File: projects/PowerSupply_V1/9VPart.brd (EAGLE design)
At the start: 49.5 x 58.4 mm, 24 parts, among them IC1 LM2596T, IC2 LM2596T, X1 IN, X2 OUT

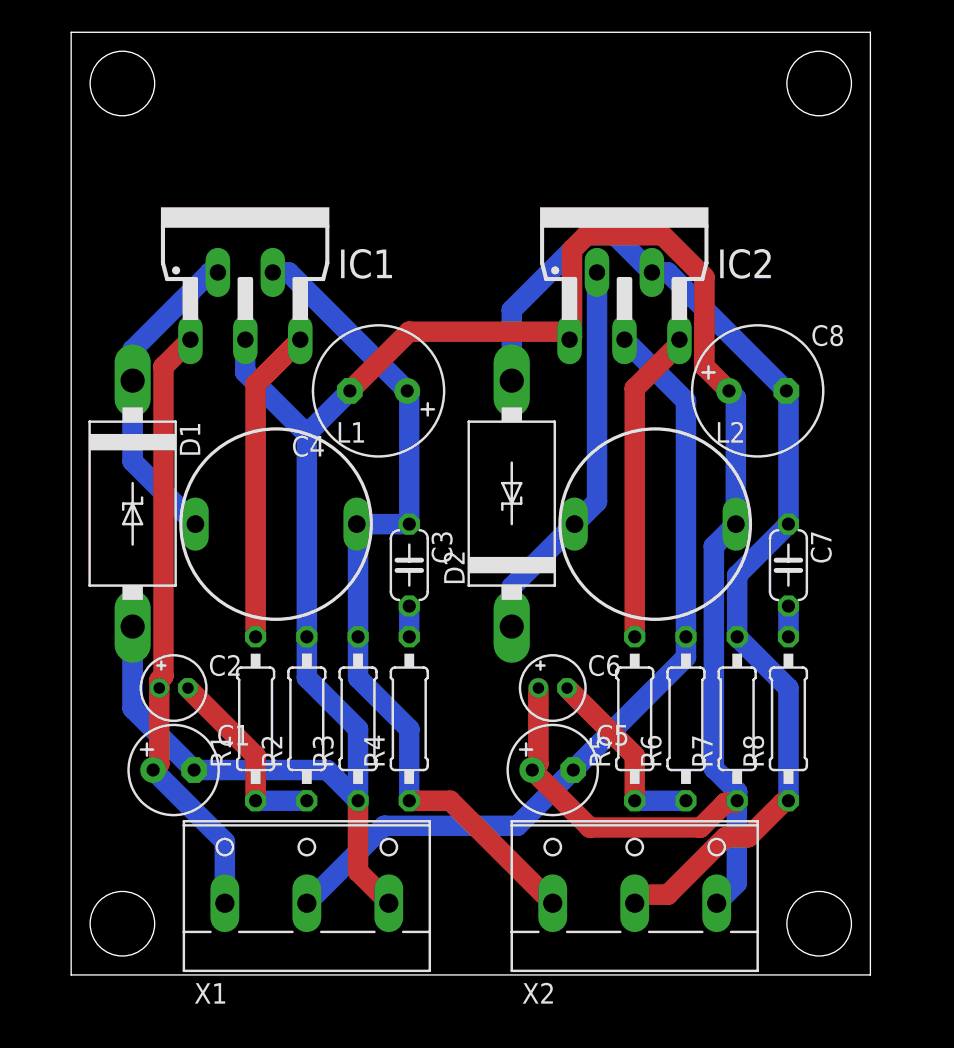
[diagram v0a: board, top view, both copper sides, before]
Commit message: refactor(all): schematics and routing changed
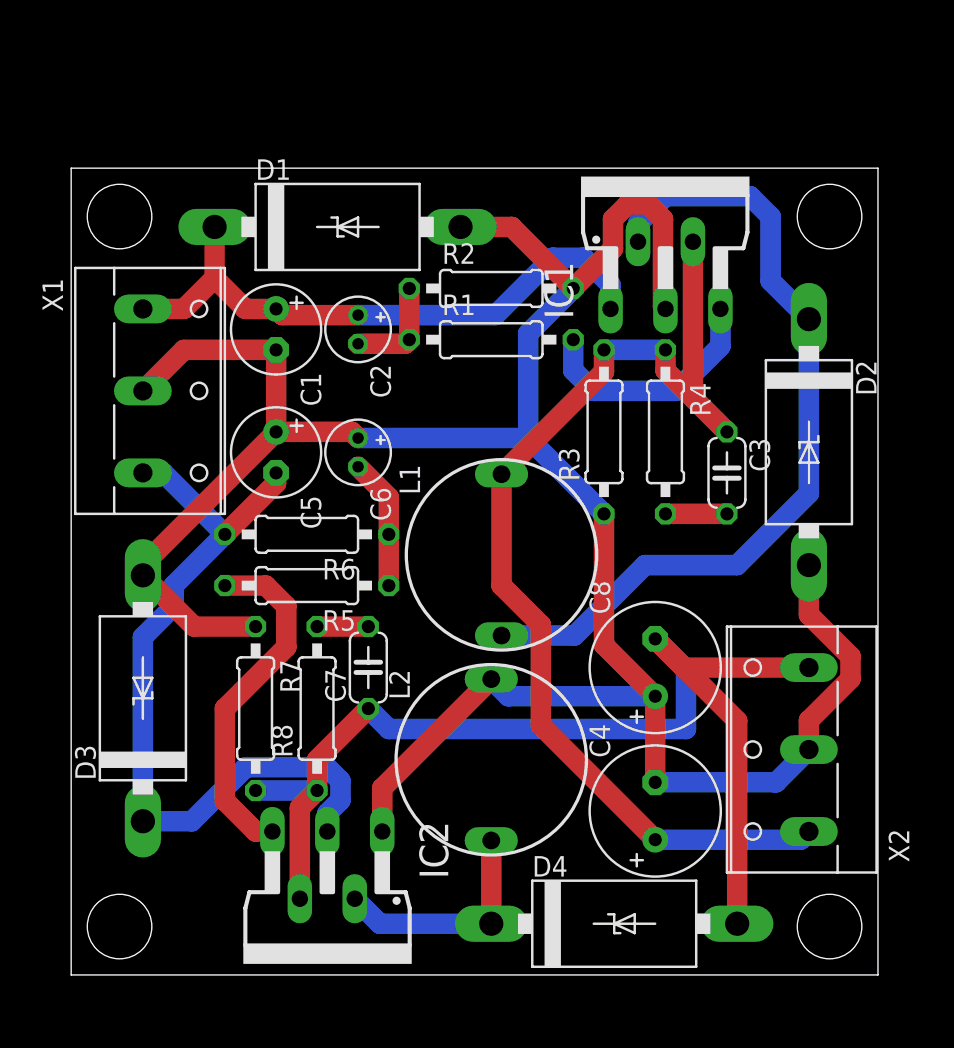
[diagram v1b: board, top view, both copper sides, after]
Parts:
- added D3, D4: 1N5822, diode:C4111-15
- C4: value 330µF -> 220µF
- C8: value 470µF -> 330µF
- moved IC2 44.6 mm to (15.9, 3.81), turned to 180 degrees
- moved X1 32.5 mm to (5.08, 36.2), turned to 270 degrees
- moved C4 31.2 mm to (36.2, 10.2), turned to 90 degrees
- moved R7 29.9 mm to (11.4, 16.5), turned to 270 degrees
- moved R8 29.2 mm to (15.2, 16.5)
- moved R2 29.0 mm to (26.0, 42.5), turned to 0 degrees
- moved C1 28.0 mm to (12.7, 40.0), turned to 270 degrees
- moved R1 27.7 mm to (26.0, 39.4), turned to 0 degrees
- moved C7 26.8 mm to (18.4, 19.1), turned to 90 degrees
- moved R6 26.1 mm to (14.6, 27.3), turned to 180 degrees
- moved C5 26.1 mm to (12.7, 32.4), turned to 270 degrees
- moved IC1 26.1 mm to (36.8, 46.4)
- moved C2 25.0 mm to (17.8, 40.0), turned to 270 degrees
- moved R4 23.8 mm to (36.8, 33.7), turned to 270 degrees
- moved R3 23.4 mm to (33.0, 33.7)
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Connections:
- net +12V renamed +9V
- removed net -12V: C7.1, C8.-, D2.A, IC2.4, R7.2, R8.1, X2.2
- new net -9V: C7.1, C8.-, D4.A, IC2.4, R7.2, R8.1, X2.3
- net +24V: now also D1.C
- net -24V: now also D3.C, X1.3; no longer X1.2
- net GND: now also D2.A, D3.A, X1.2, X2.2; no longer X1.3, X2.3
- net N$2: now also D4.C; no longer D2.C
- net N$3: now also D2.C; no longer D1.C
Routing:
- net -9V: track 0.00 -> 76.5 mm
- net -12V: track 67.5 -> 0.00 mm
- net N$3: track 19.7 -> 51.4 mm
- net +9V: track 52.9 -> 69.8 mm
- net N$2: track 24.1 -> 14.3 mm
- net N$6: track 11.9 -> 6.46 mm
- net N$4: track 19.6 -> 15.0 mm
- net N$8: track 11.9 -> 8.16 mm
- net N$7: track 19.6 -> 21.7 mm
- net -24V: track 51.1 -> 49.1 mm
- net N$1: track 1.91 -> 3.81 mm
- net N$5: track 1.91 -> 3.17 mm
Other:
- board size 49.5 x 58.4 mm -> 50 x 50 mm

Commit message: feat: 9VPart refactored
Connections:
- net +24V renamed +20V
- net -24V renamed -20V
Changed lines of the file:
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@@
 <wire x1="36.83" y1="28.575" x2="40.64" y2="28.575" width="1.27" layer="1"/>
-</signal>
-<signal name="+24V">
-<contactref element="X1" pad="1"/>
-<contactref element="C1" pad="+"/>
-<contactref element="IC1" pad="1"/>
-<contactref element="C2" pad="+"/>
-<contactref element="D1" pad="C"/>
-<wire x1="8.89" y1="45.72" x2="8.89" y2="46.355" width="1.27" layer="1"/>
-<wire x1="8.89" y1="43.18" x2="10.795" y2="41.275" width="1.27" layer="1"/>
-<wire x1="10.795" y1="41.275" x2="12.7" y2="41.275" width="1.27" layer="1"/>
-<wire x1="8.89" y1="46.355" x2="8.89" y2="43.18" width="1.27" layer="1"/>
-<wire x1="4.445" y1="41.275" x2="6.985" y2="41.275" width="1.27" layer="1"/>
-<wire x1="6.985" y1="41.275" x2="8.89" y2="43.18" width="1.27" layer="1"/>
-<wire x1="17.78" y1="40.894" x2="13.081" y2="40.894" width="1.27" layer="1"/>
-<wire x1="13.081" y1="40.894" x2="12.7" y2="41.275" width="1.27" layer="1"/>
-<wire x1="17.78" y1="40.894" x2="26.289" y2="40.894" width="1.27" layer="16"/>
-<wire x1="26.289" y1="40.894" x2="29.845" y2="44.45" width="1.27" layer="16"/>
-<wire x1="29.845" y1="44.45" x2="31.75" y2="44.45" width="1.27" layer="16"/>
-<wire x1="31.75" y1="44.45" x2="33.4264" y2="42.7736" width="1.27" layer="16"/>
-<wire x1="33.4264" y1="42.7736" x2="33.4264" y2="41.275" width="1.27" layer="16"/>
-</signal>
-<signal name="-24V">
-<contactref element="C5" pad="-"/>
-<contactref element="R6" pad="2"/>
-<contactref element="IC2" pad="3"/>
-<contactref element="D3" pad="C"/>
-<contactref element="X1" pad="3"/>
-<wire x1="9.525" y1="27.305" x2="12.7" y2="30.48" width="1.27" layer="1"/>
-<wire x1="12.7" y1="30.48" x2="12.7" y2="31.115" width="1.27" layer="1"/>
-<wire x1="16.6878" y1="10.8303" x2="16.6878" y2="12.0297" width="1.27" layer="16"/>
-<wire x1="16.6878" y1="12.0297" x2="15.8397" y2="12.8778" width="1.27" layer="16"/>
-<wire x1="7.4775" y1="9.525" x2="4.445" y2="9.525" width="1.27" layer="16"/>
-<wire x1="15.8397" y1="12.8778" x2="10.8303" y2="12.8778" width="1.27" layer="16"/>
-<wire x1="10.8303" y1="12.8778" x2="7.4775" y2="9.525" width="1.27" layer="16"/>
-<wire x1="15.875" y1="8.89" x2="15.875" y2="10.0175" width="1.27" layer="16"/>
-<wire x1="15.875" y1="10.0175" x2="16.6878" y2="10.8303" width="1.27" layer="16"/>
-<wire x1="4.445" y1="31.115" x2="5.715" y2="31.115" width="1.27" layer="16"/>
-<wire x1="5.715" y1="31.115" x2="9.525" y2="27.305" width="1.27" layer="16"/>
-<wire x1="9.525" y1="27.305" x2="6.35635" y2="24.13635" width="1.27" layer="16"/>
-<wire x1="6.35635" y1="24.13635" x2="6.35635" y2="22.8493375" width="1.27" layer="16"/>
-<wire x1="4.445" y1="20.9379875" x2="4.445" y2="9.525" width="1.27" layer="16"/>
-<wire x1="6.35635" y1="22.8493375" x2="4.445" y2="20.9379875" width="1.27" layer="16"/>
 </signal>
 <signal name="N$4">
@@
 <wire x1="29.1074" y1="15.4696" x2="36.195" y2="8.382" width="1.27" layer="1"/>
 <wire x1="29.1074" y1="21.70288125" x2="29.1074" y2="15.4696" width="1.27" layer="1"/>
-<wire x1="45.212" y1="8.382" x2="36.195" y2="8.382" width="1.27" layer="16"/>
 <wire x1="33.02" y1="38.735" x2="36.83" y2="38.735" width="1.27" layer="16"/>
 <wire x1="45.72" y1="8.89" x2="45.212" y2="8.382" width="1.27" layer="16"/>
+<wire x1="45.212" y1="8.382" x2="36.195" y2="8.382" width="1.27" layer="16"/>
 </signal>
 <signal name="-9V">
@@
 <wire x1="37.973" y1="19.05" x2="36.195" y2="20.828" width="1.27" layer="1"/>
 </signal>
+<signal name="+20V">
+<contactref element="X1" pad="1"/>
+<contactref element="C1" pad="+"/>
+<contactref element="IC1" pad="1"/>
+<contactref element="C2" pad="+"/>
+<contactref element="D1" pad="C"/>
+<wire x1="8.89" y1="45.72" x2="8.89" y2="46.355" width="1.27" layer="1"/>
+<wire x1="8.89" y1="43.18" x2="10.795" y2="41.275" width="1.27" layer="1"/>
+<wire x1="10.795" y1="41.275" x2="12.7" y2="41.275" width="1.27" layer="1"/>
+<wire x1="8.89" y1="46.355" x2="8.89" y2="43.18" width="1.27" layer="1"/>
+<wire x1="6.985" y1="41.275" x2="8.89" y2="43.18" width="1.27" layer="1"/>
+<wire x1="17.78" y1="40.894" x2="13.081" y2="40.894" width="1.27" layer="1"/>
+<wire x1="13.081" y1="40.894" x2="12.7" y2="41.275" width="1.27" layer="1"/>
+<wire x1="17.78" y1="40.894" x2="26.289" y2="40.894" width="1.27" layer="16"/>
+<wire x1="26.289" y1="40.894" x2="29.845" y2="44.45" width="1.27" layer="16"/>
+<wire x1="29.845" y1="44.45" x2="31.75" y2="44.45" width="1.27" layer="16"/>
+<wire x1="31.75" y1="44.45" x2="33.4264" y2="42.7736" width="1.27" layer="16"/>
+<wire x1="33.4264" y1="42.7736" x2="33.4264" y2="41.275" width="1.27" layer="16"/>
+<wire x1="4.445" y1="41.275" x2="6.985" y2="41.275" width="1.27" layer="1"/>
+</signal>
+<signal name="-20V">
+<contactref element="X1" pad="3"/>
+<contactref element="D3" pad="C"/>
+<contactref element="C5" pad="-"/>
+<contactref element="R6" pad="2"/>
+<contactref element="IC2" pad="3"/>
+<wire x1="12.7" y1="30.48" x2="9.525" y2="27.305" width="1.27" layer="1"/>
+<wire x1="16.6878" y1="10.8303" x2="16.6878" y2="12.0297" width="1.27" layer="16"/>
+<wire x1="16.6878" y1="12.0297" x2="15.8397" y2="12.8778" width="1.27" layer="16"/>
+<wire x1="15.8397" y1="12.8778" x2="10.8303" y2="12.8778" width="1.27" layer="16"/>
+<wire x1="10.8303" y1="12.8778" x2="7.4775" y2="9.525" width="1.27" layer="16"/>
+<wire x1="15.875" y1="8.89" x2="15.875" y2="10.0175" width="1.27" layer="16"/>
+<wire x1="15.875" y1="10.0175" x2="16.6878" y2="10.8303" width="1.27" layer="16"/>
+<wire x1="5.715" y1="31.115" x2="9.525" y2="27.305" width="1.27" layer="16"/>
+<wire x1="9.525" y1="27.305" x2="6.35635" y2="24.13635" width="1.27" layer="16"/>
+<wire x1="6.35635" y1="24.13635" x2="6.35635" y2="22.8493375" width="1.27" layer="16"/>
+<wire x1="4.445" y1="20.9379875" x2="6.35635" y2="22.8493375" width="1.27" layer="16"/>
+<wire x1="12.7" y1="31.115" x2="12.7" y2="30.48" width="1.27" layer="1"/>
+<wire x1="4.445" y1="31.115" x2="5.715" y2="31.115" width="1.27" layer="16"/>
+<wire x1="4.445" y1="9.525" x2="4.445" y2="20.9379875" width="1.27" layer="16"/>
+<wire x1="7.4775" y1="9.525" x2="4.445" y2="9.525" width="1.27" layer="16"/>
+</signal>
 </signals>

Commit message: feat: small fixes and changes applied
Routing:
- net -9V: track 76.5 -> 71.4 mm
- net +20V: track 38.2 -> 37.6 mm
